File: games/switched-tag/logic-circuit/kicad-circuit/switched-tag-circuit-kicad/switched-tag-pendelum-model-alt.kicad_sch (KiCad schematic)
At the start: 7 parts

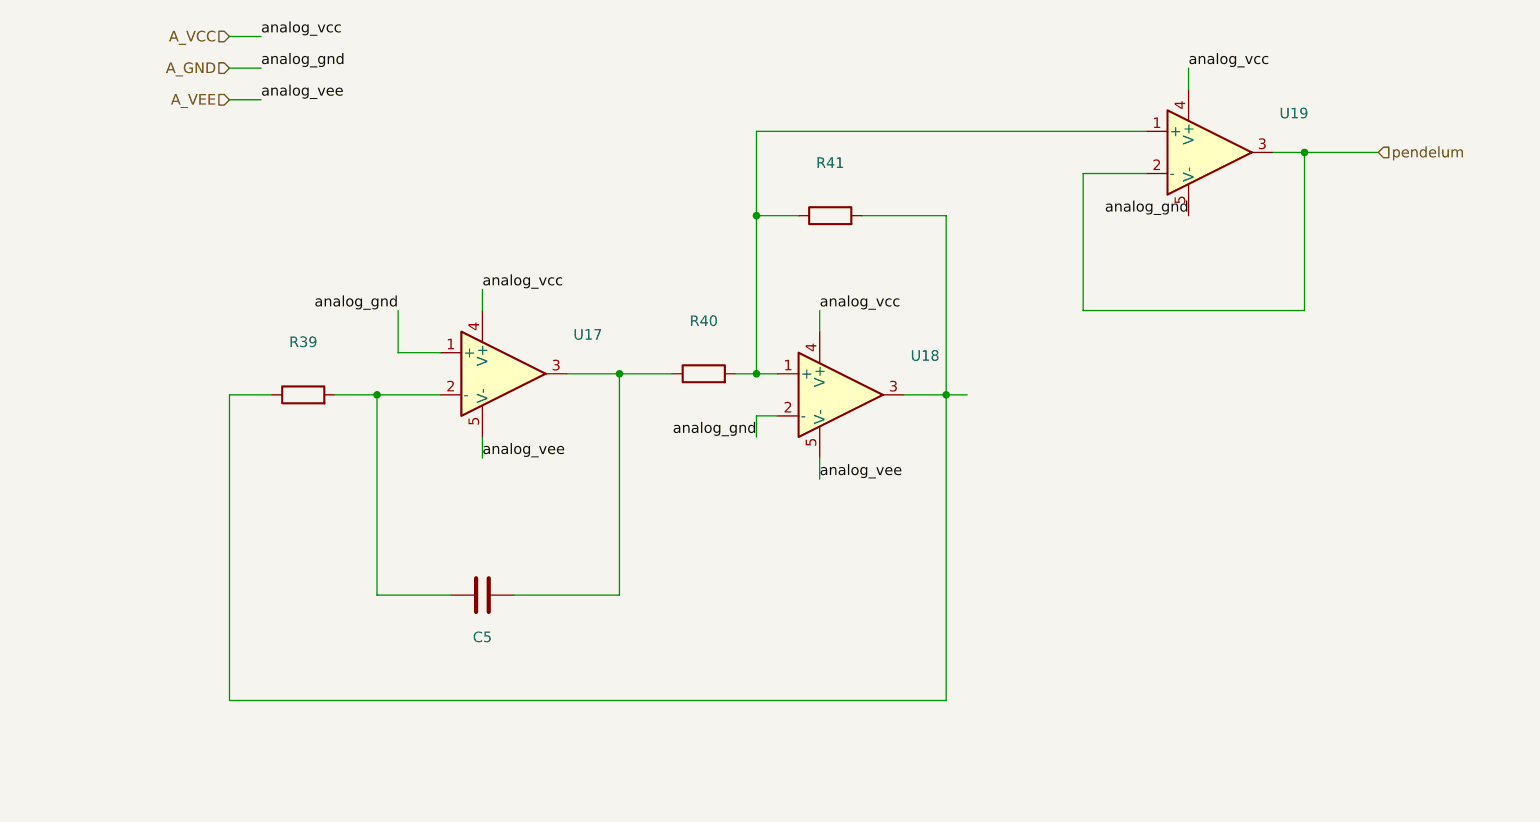
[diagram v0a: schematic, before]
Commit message: Changed spice model of opamp in kicad sim. Fixed design error in it player determination in ltspice and kicad schematic
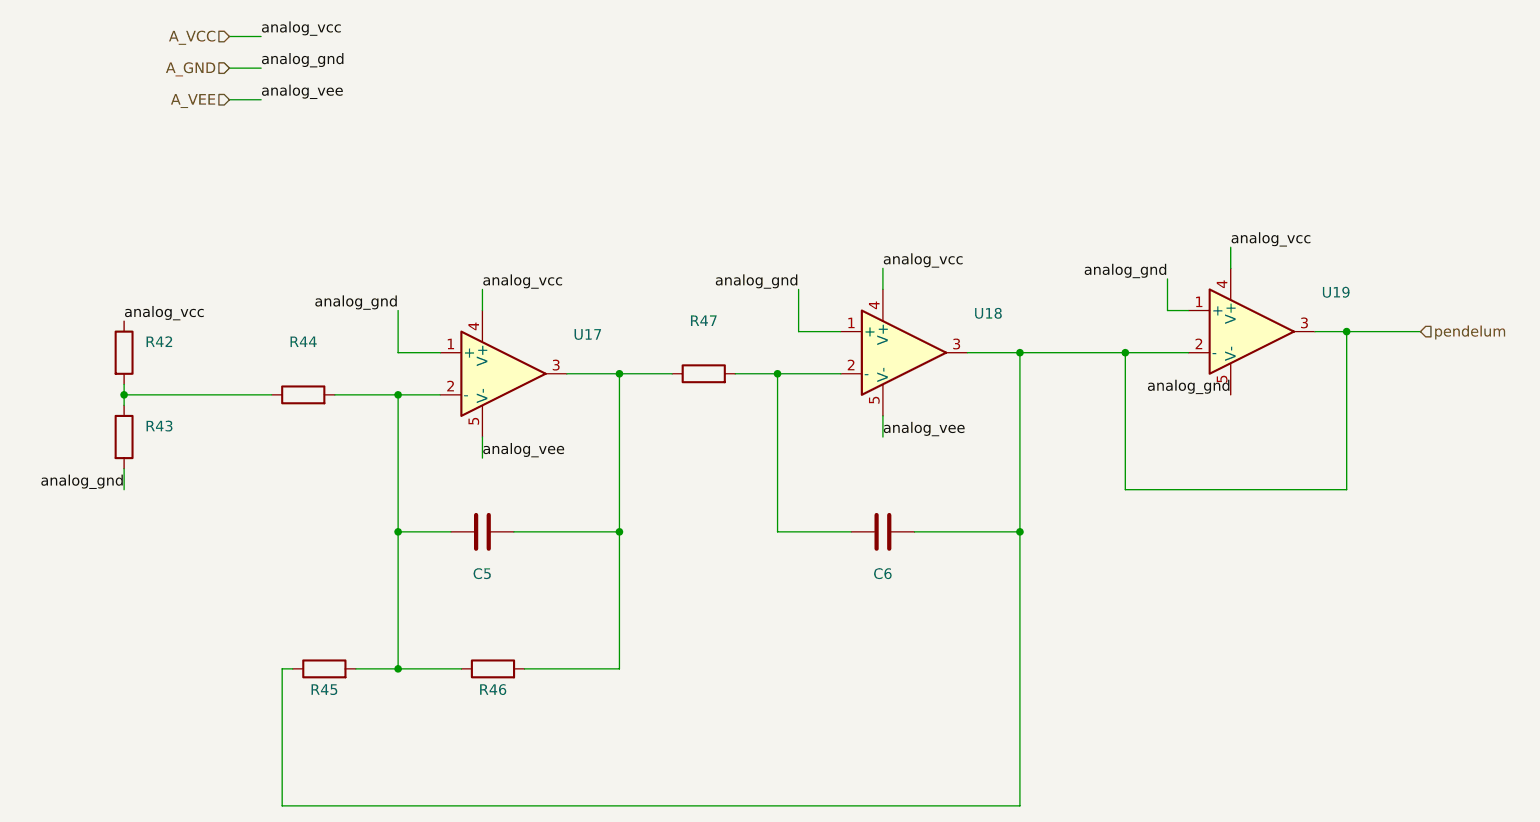
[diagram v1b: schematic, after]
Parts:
- removed R41: (no value), symbol Device:R
- added C6: (no value), symbol Device:C
- added R42, R43, R45, R46: (no value), symbol Device:R
- U17, U19: Spice_Lib_File /home/pab/Inventions/analog-circuit-game-console/ms-circuit-video-games/spice-models/ada4692.mod -> /home/pab/Inventions/analog-circuit-game-console/ms-circuit-video-games/spice-models/LM358-onsemi.mod; Spice_Model ADA4692 -> LM358
- U18: value (none) -> ~; Spice_Lib_File /home/pab/Inventions/analog-circuit-game-console/ms-circuit-video-games/spice-models/ada4692.mod -> /home/pab/Inventions/analog-circuit-game-console/ms-circuit-video-games/spice-models/LM358-onsemi.mod; Spice_Model ADA4692 -> LM358
- renumbered R39 to R44, R40 to R47
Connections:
- net A_GND: now also U18.1 (+), U19.1 (+), R43.2; no longer U18.2 (-)
- net A_VCC: now also R42.1
- net pendelum: now also U18.3, C6.2, R45.1
- net at R44.1: now also R42.2, R43.1; no longer U18.3
- net at C5.1, R44.2, U17.2 (-): now also R45.2, R46.1
- net at C5.2, R47.1, U17.3: now also R46.2
- new net: C6.1, R47.2, U18.2 (-)
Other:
- moved on the sheet: C5, U19
